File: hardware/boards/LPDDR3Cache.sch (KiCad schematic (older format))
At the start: 1 part, among them U1 ECP5UM5G-381caBGA

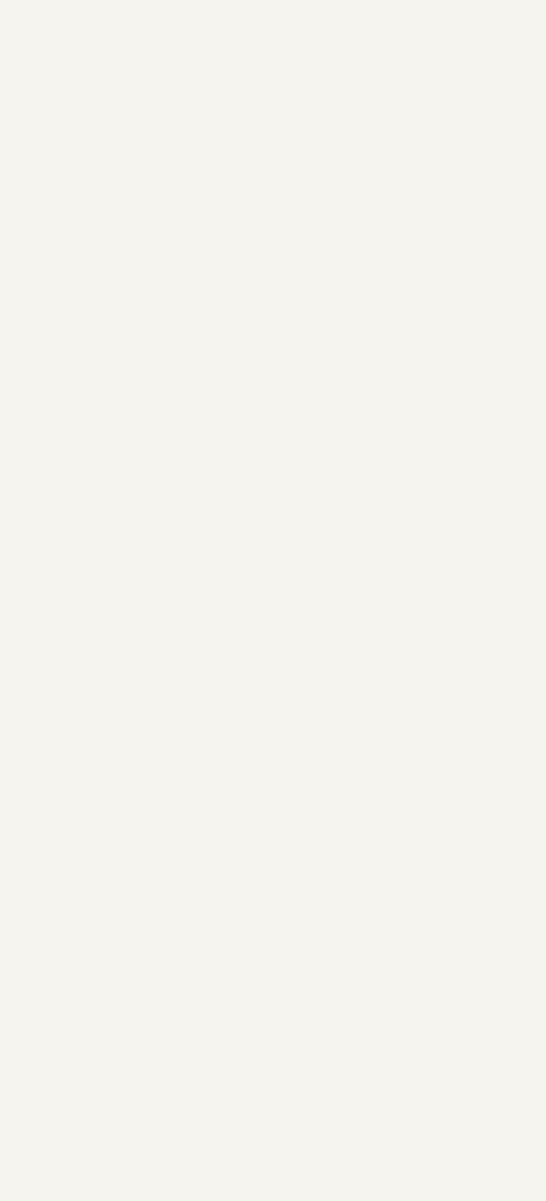
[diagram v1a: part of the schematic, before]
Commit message: Added the DDR3 Module
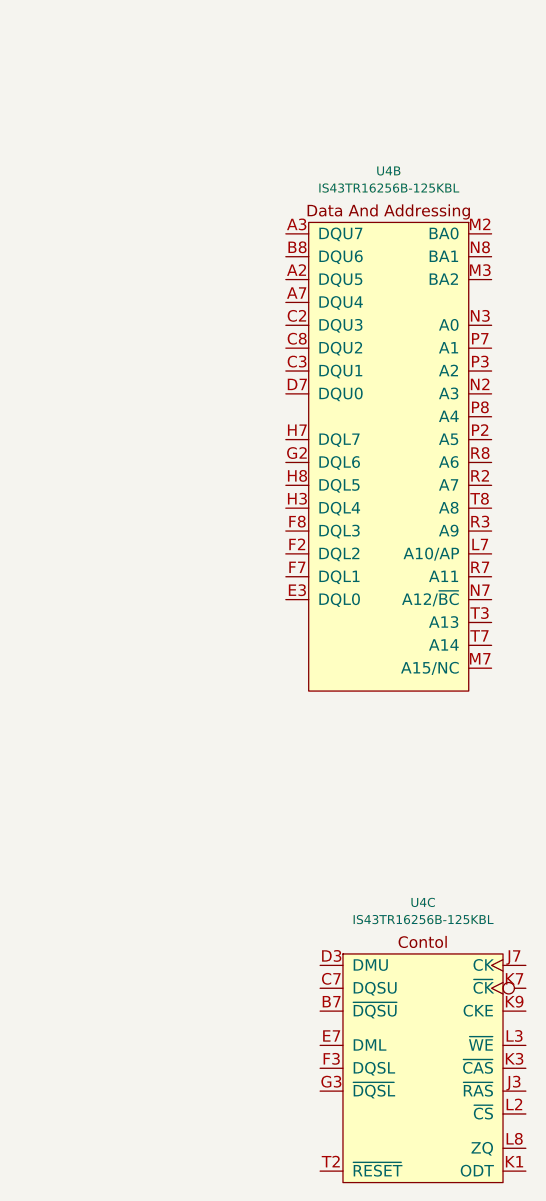
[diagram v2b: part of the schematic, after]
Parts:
- added U4: IS43TR16256B-125KBL, Package_BGA:BGA-96_9.0x13.0mm_Layout2x3x16_P0.8mm, symbol lethalbit-memory:IS43TR16256B-125KBL
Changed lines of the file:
@@
 $Descr A3 16535 11693
 encoding utf-8
-Sheet 4 11
+Sheet 2 11
 Title "lethallink"
 Date "2020-06-13"
@@
 NoConn ~ 6800 4000
 NoConn ~ 6800 3900
+$Comp
+L lethalbit-memory:IS43TR16256B-125KBL U4
+U 2 1 5F1DEF98
+P 9900 3200
+F 0 "U4" H 9900 3674 39  0000 C CNN
+F 1 "IS43TR16256B-125KBL" H 9900 3599 39  0000 C CNN
+F 2 "Package_BGA:BGA-96_9.0x13.0mm_Layout2x3x16_P0.8mm" H 9900 3600 39  0001 C CNN
+F 3 "http://www.issi.com/WW/pdf/43-46TR16256B-85120BL.pdf" H 9900 3600 39  0001 C CNN
+F 4 "ISSI" H 9900 3200 50  0001 C CNN "MFR"
+F 5 "IS43TR16256B-125KBL" H 9900 3200 50  0001 C CNN "MPN"
+	2    9900 3200
+	1    0    0    -1
+$EndComp
+$Comp
+L lethalbit-memory:IS43TR16256B-125KBL U4
+U 3 1 5F1E0638
+P 10050 6400
+F 0 "U4" H 10050 6874 39  0000 C CNN
+F 1 "IS43TR16256B-125KBL" H 10050 6799 39  0000 C CNN
+F 2 "Package_BGA:BGA-96_9.0x13.0mm_Layout2x3x16_P0.8mm" H 10050 6800 39  0001 C CNN
+F 3 "http://www.issi.com/WW/pdf/43-46TR16256B-85120BL.pdf" H 10050 6800 39  0001 C CNN
+F 4 "ISSI" H 10050 6400 50  0001 C CNN "MFR"
+F 5 "IS43TR16256B-125KBL" H 10050 6400 50  0001 C CNN "MPN"
+	3    10050 6400
+	1    0    0    -1
+$EndComp
 $EndSCHEMATC
